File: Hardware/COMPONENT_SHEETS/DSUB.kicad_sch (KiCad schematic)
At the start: 3 parts, among them J3 L717SDC37P1ACH4F

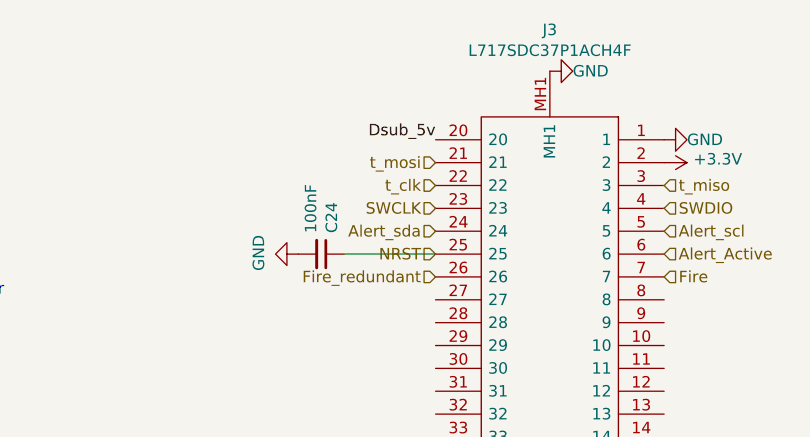
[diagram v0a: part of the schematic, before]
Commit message: Corrected PCB edge cuts, removed components
Will be mimicking layout done by Seth Sievers
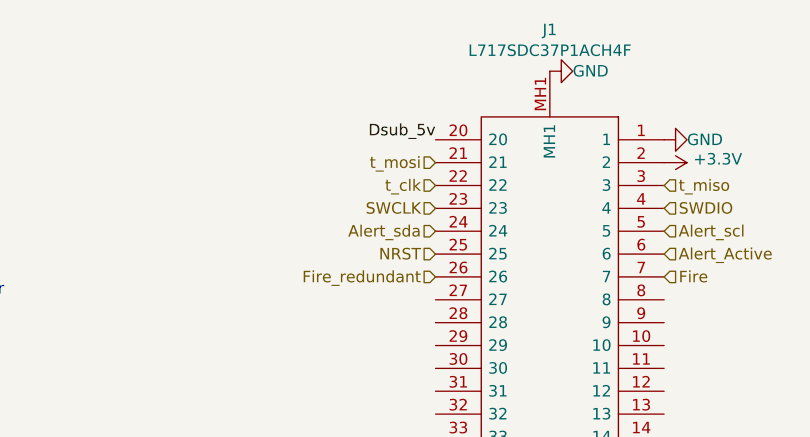
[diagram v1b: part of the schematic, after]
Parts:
- removed C24: 100nF, Capacitor_SMD:C_0603_1608Metric_Pad1.08x0.95mm_HandSolder, symbol Device:C_Small
- renumbered J3 to J1
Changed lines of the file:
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@@
-    (stroke (width 0) (type default) (color 0 0 0 0))
-  )
-  (wire (pts (xy 134.62 60.96) (xy 144.78 60.96))
     (stroke (width 0) (type default) (color 0 0 0 0))
   )
@@
   (symbol (lib_id "power:+3.3V") (at 170.18 50.8 270) (mirror x) (unit 1)
     (in_bom yes) (on_board yes)
-    (property "Reference" "#PWR0122" (id 0) (at 166.37 50.8 0)
+    (property "Reference" "#PWR09" (id 0) (at 166.37 50.8 0)
       (effects (font (size 1.27 1.27)) hide)
     )
@@
   (symbol (lib_id "power:+3.3V") (at 170.18 91.44 270) (mirror x) (unit 1)
     (in_bom yes) (on_board yes)
-    (property "Reference" "#PWR0124" (id 0) (at 166.37 91.44 0)
+    (property "Reference" "#PWR010" (id 0) (at 166.37 91.44 0)
       (effects (font (size 1.27 1.27)) hide)
     )
@@
     )
     (property "Datasheet" "" (id 3) (at 170.18 91.44 0)
-      (effects (font (size 1.27 1.27)) hide)
-    )
-    (pin "1")
-  )
-  (symbol (lib_id "Device:C_Small") (at 132.08 60.96 270) (mirror x)
-    (in_bom yes) (on_board yes)
-    (property "Reference" "C24" (id 0) (at 133.2484 58.6232 0)
-      (effects (font (size 1.27 1.27)) (justify left))
-    )
-    (property "Value" "100nF" (id 1) (at 130.937 58.6232 0)
-      (effects (font (size 1.27 1.27)) (justify left))
-    )
-    (property "Footprint" "Capacitor_SMD:C_0603_1608Metric_Pad1.08x0.95mm_HandSolder" (id 2) (at 132.08 60.96 0)
-      (effects (font (size 1.27 1.27)) hide)
-    )
-    (property "Datasheet" "~" (id 3) (at 132.08 60.96 0)
-      (effects (font (size 1.27 1.27)) hide)
-    )
-    (pin "1")
-    (pin "2")
-  )
-  (symbol (lib_id "power:GND") (at 129.54 60.96 270) (mirror x)
-    (in_bom yes) (on_board yes)
-    (property "Reference" "#PWR0101" (id 0) (at 123.19 60.96 0)
-      (effects (font (size 1.27 1.27)) hide)
-    )
-    (property "Value" "GND" (id 1) (at 125.1458 60.833 0))
-    (property "Footprint" "" (id 2) (at 129.54 60.96 0)
-      (effects (font (size 1.27 1.27)) hide)
-    )
-    (property "Datasheet" "" (id 3) (at 129.54 60.96 0)
       (effects (font (size 1.27 1.27)) hide)
     )
@@
   (symbol (lib_id "power:+5V") (at 54.61 81.28 0) (unit 1)
     (in_bom yes) (on_board yes)
-    (property "Reference" "#PWR0123" (id 0) (at 54.61 85.09 0)
+    (property "Reference" "#PWR05" (id 0) (at 54.61 85.09 0)
       (effects (font (size 1.27 1.27)) hide)
     )
@@
   (symbol (lib_id "power:GND") (at 173.99 93.98 0) (unit 1)
     (in_bom yes) (on_board yes)
-    (property "Reference" "#PWR0127" (id 0) (at 173.99 100.33 0)
+    (property "Reference" "#PWR011" (id 0) (at 173.99 100.33 0)
       (effects (font (size 1.27 1.27)) hide)
     )
@@
   (symbol (lib_id "power:GND") (at 157.48 40.64 90) (unit 1)
     (in_bom yes) (on_board yes)
-    (property "Reference" "#PWR0125" (id 0) (at 163.83 40.64 0)
+    (property "Reference" "#PWR06" (id 0) (at 163.83 40.64 0)
       (effects (font (size 1.27 1.27)) hide)
     )
@@
   (symbol (lib_id "Data_Collection_KiCAD_Project-rescue:L717SDC37P1ACH4F-SamacSys_Parts-Charges_KiCAD_Project-rescue") (at 157.48 40.64 270)
     (in_bom yes) (on_board yes)
-    (property "Reference" "J3" (id 0) (at 157.48 36.0426 90))
+    (property "Reference" "J1" (id 0) (at 157.48 36.0426 90))
     (property "Value" "L717SDC37P1ACH4F" (id 1) (at 157.48 38.354 90))
     (property "Footprint" "RDT_Custom_Footprints:L717SDC37P1ACH4F" (id 2) (at 165.1 97.79 0)
@@
   (symbol (lib_id "power:GND") (at 170.18 48.26 90) (unit 1)
     (in_bom yes) (on_board yes)
-    (property "Reference" "#PWR0126" (id 0) (at 176.53 48.26 0)
+    (property "Reference" "#PWR08" (id 0) (at 176.53 48.26 0)
       (effects (font (size 1.27 1.27)) hide)
     )
@@
   (symbol (lib_id "power:GND") (at 157.48 101.6 0) (unit 1)
     (in_bom yes) (on_board yes)
-    (property "Reference" "#PWR0128" (id 0) (at 157.48 107.95 0)
-      (effects (font (size 1.27 1.27)) hide)
-    )
+    (property "Reference" "#PWR07" (id 0) (at 157.48 107.95 0)
+      (effects (font (size 1.27 1.27)) hide)
+    )

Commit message: wtf is wrong with my github install
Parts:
- JP1: footprint Jumper:SolderJumper-2_P1.3mm_Bridged_Pad1.0x1.5mm -> Jumper:SolderJumper-2_P1.3mm_Open_Pad1.0x1.5mm
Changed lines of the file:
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@@
     (property "Reference" "JP1" (id 0) (at 69.85 76.073 0))
     (property "Value" "5V Disconnect" (id 1) (at 69.85 78.3844 0))
-    (property "Footprint" "Jumper:SolderJumper-2_P1.3mm_Bridged_Pad1.0x1.5mm" (id 2) (at 69.85 81.28 0)
+    (property "Footprint" "Jumper:SolderJumper-2_P1.3mm_Open_Pad1.0x1.5mm" (id 2) (at 69.85 81.28 0)
       (effects (font (size 1.27 1.27)) hide)
     )
